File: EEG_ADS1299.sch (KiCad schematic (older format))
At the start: 76 parts, among them IC1 ADS1299, P1 CONN_2, P2 CONN_2, P3 CONN_01X08, U1 TPS2294x, U2 TPS61222, U3 NRF528XX-QFAA, U4 MPU-9250, U5 INA828, U6 INA828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

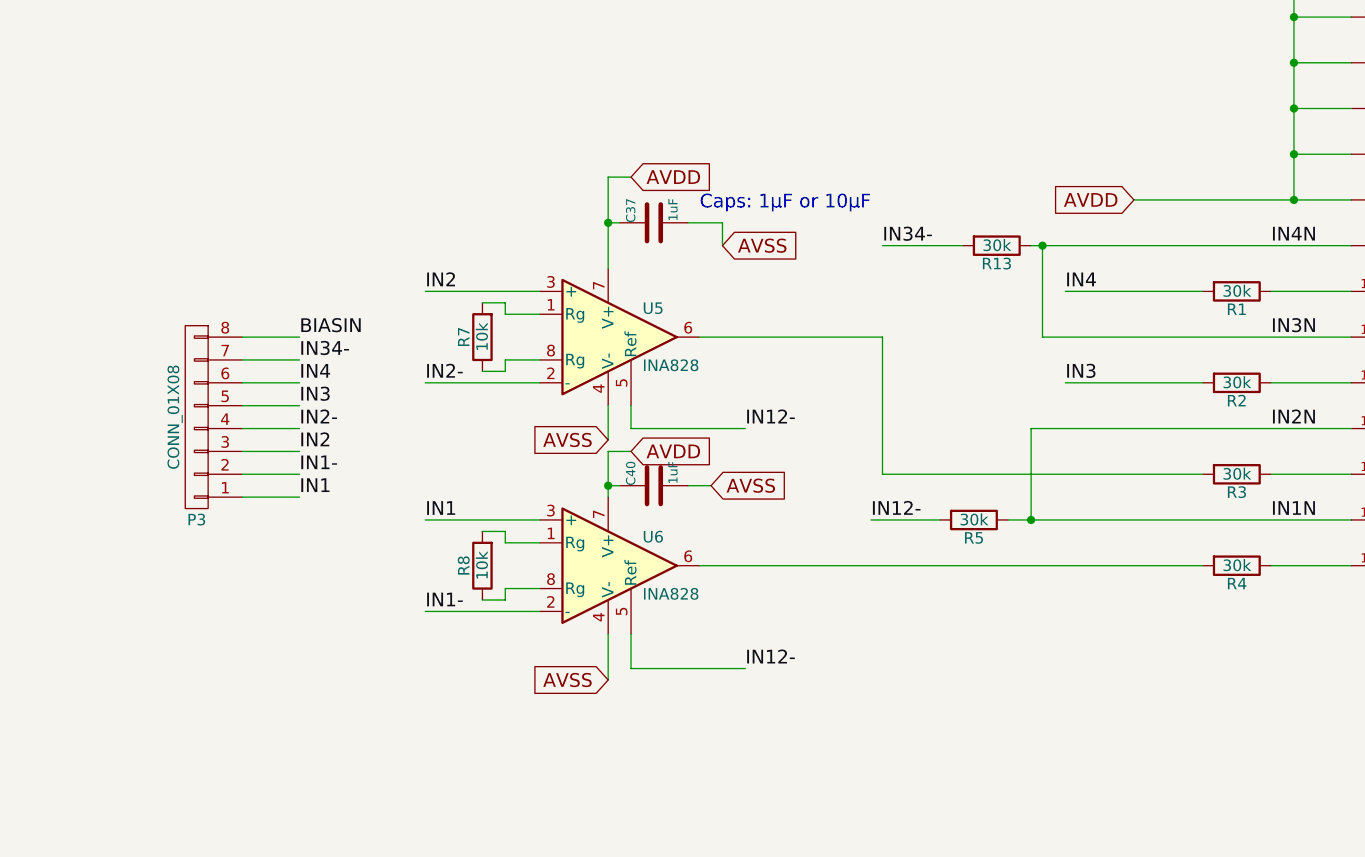
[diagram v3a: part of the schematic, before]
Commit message: Update Schematic for ADS1299/INA828 Removing INA828 from circuit. Shorting negative inputs in pairs.
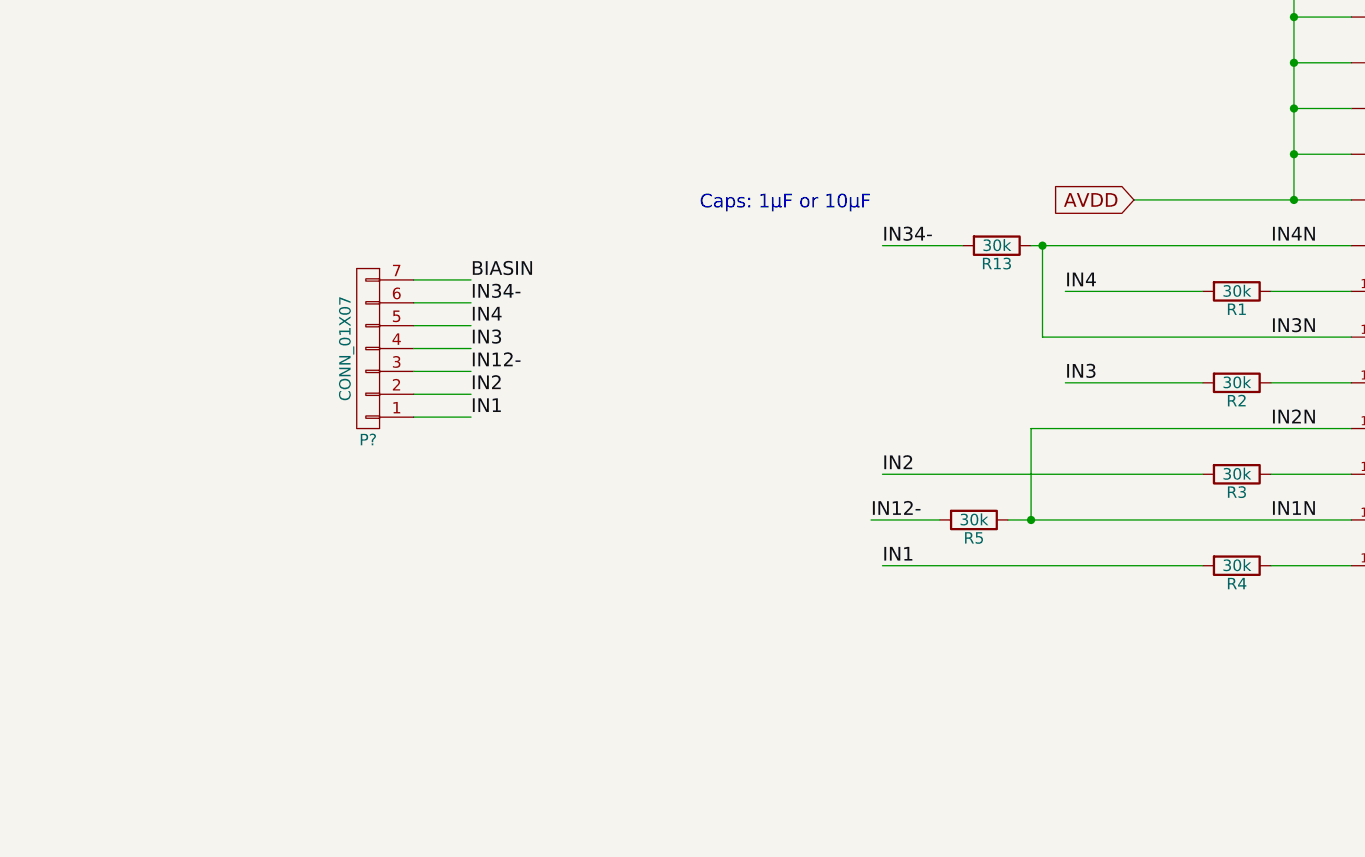
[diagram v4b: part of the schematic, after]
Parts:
- removed C37, C40: 1uF, Capacitors_SMD:C_0402, symbol C
- removed P3: CONN_01X08, symbol CONN_01X08
- removed R7, R8: 10k, Resistors_SMD:R_0402, symbol R
- removed U5, U6: INA828, INA828:SOIC_8_4.9mm_x_3.91, symbol INA128
- added P?: CONN_01X07, symbol CONN_01X07
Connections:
- net BIASIN: now also P?.7 (P7)
- net IN1: now also R4.2, P?.1 (P1)
- net IN12-: now also P?.3 (P3)
- net IN2: now also R3.2, P?.2 (P2)
- net IN3: now also P?.4 (P4)
- net IN34-: now also P?.6 (P6)
- net IN4: now also P?.5 (P5)
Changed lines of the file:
@@
 Text Label 13500 10050 0    60   ~ 0
 IN4N
-Text Label 9250 10850 0    60   ~ 0
-IN2-
-Text Label 9250 11050 0    60   ~ 0
-IN1-
 $Comp
 L NRF528XX-QFAA-RESCUE-EEG_ADS1299_2 U3
@@
 Text Label 11750 11250 0    60   ~ 0
 IN12-
-$Comp
-L INA128 U5
-U 1 1 5A26481D
-P 10600 10450
-F 0 "U5" H 10750 10575 50  0000 L CNN
-F 1 "INA828" H 10750 10325 50  0000 L CNN
-F 2 "INA828:SOIC_8_4.9mm_x_3.91" H 10700 10450 50  0001 C CNN
-F 3 "" H 10700 10450 50  0001 C CNN
-	1    10600 10450
-	1    0    0    -1
-$EndComp
-$Comp
-L INA128 U6
-U 1 1 5A265779
-P 10600 11450
-F 0 "U6" H 10750 11575 50  0000 L CNN
-F 1 "INA828" H 10750 11325 50  0000 L CNN
-F 2 "INA828:SOIC_8_4.9mm_x_3.91" H 10700 11450 50  0001 C CNN
-F 3 "" H 10700 11450 50  0001 C CNN
-	1    10600 11450
-	1    0    0    -1
-$EndComp
-Text GLabel 10600 10900 0    60   Input ~ 0
-AVSS
-Text GLabel 10600 11950 0    60   Input ~ 0
-AVSS
-Text GLabel 10700 10950 2    60   Input ~ 0
-AVDD
-Text GLabel 10700 9750 2    60   Input ~ 0
-AVDD
-$Comp
-L R R7
-U 1 1 5A26B635
-P 10050 10450
-F 0 "R7" V 10130 10450 50  0000 C CNN
-F 1 "10k" V 10050 10450 50  0000 C CNN
-F 2 "Resistors_SMD:R_0402" V 9980 10450 50  0001 C CNN
-F 3 "" H 10050 10450 50  0000 C CNN
-	1    10050 10450
-	-1   0    0    1
-$EndComp
-$Comp
-L R R8
-U 1 1 5A26CFB1
-P 10050 11450
-F 0 "R8" V 10130 11450 50  0000 C CNN
-F 1 "10k" V 10050 11450 50  0000 C CNN
-F 2 "Resistors_SMD:R_0402" V 9980 11450 50  0001 C CNN
-F 3 "" H 10050 11450 50  0000 C CNN
-	1    10050 11450
-	-1   0    0    1
-$EndComp
-Text Label 9800 11250 0    60   ~ 0
+Text Label 10000 10500 0    60   ~ 0
+IN3
+Text Label 10000 10700 0    60   ~ 0
+IN2
+Text Label 10000 10800 0    60   ~ 0
 IN1
-Text Label 9800 10250 0    60   ~ 0
-IN2
-Text Label 9250 10650 0    60   ~ 0
-IN4
-Text Label 9250 10750 0    60   ~ 0
-IN3
-Text Label 9250 10950 0    60   ~ 0
-IN2
-Text Label 9250 11150 0    60   ~ 0
-IN1
-Text Label 9250 10450 0    60   ~ 0
+Text Label 10000 10200 0    60   ~ 0
 BIASIN
 Text Label 13500 10450 0    60   ~ 0
 IN3N
-$Comp
-L C C37
-U 1 1 5A28A53A
-P 10800 9950
-F 0 "C37" H 10800 10050 40  0000 L CNN
-F 1 "1uF" H 10806 9865 40  0000 L CNN
-F 2 "Capacitors_SMD:C_0402" H 10838 9800 30  0001 C CNN
-F 3 "~" H 10800 9950 60  0000 C CNN
-	1    10800 9950
-	0    -1   -1   0
-$EndComp
-Text GLabel 11100 10050 2    60   Input ~ 0
-AVSS
 Text Notes 11000 9900 0    60   ~ 0
 Caps: 1µF or 10µF
@@
 	1    0    0    -1
 $EndComp
-Wire Wire Line
-	11800 10450 11800 11050
-Wire Wire Line
-	11000 10450 11800 10450
-Wire Wire Line
-	10300 11250 9800 11250
-Wire Wire Line
-	10150 11600 10150 11550
-Wire Wire Line
-	10050 11600 10150 11600
-Wire Wire Line
-	10150 11550 10300 11550
-Wire Wire Line
-	10150 11300 10050 11300
-Wire Wire Line
-	10150 11350 10150 11300
-Wire Wire Line
-	10300 11350 10150 11350
-Wire Wire Line
-	10300 10250 9800 10250
-Wire Wire Line
-	10150 10300 10050 10300
-Wire Wire Line
-	10150 10350 10150 10300
-Wire Wire Line
-	10300 10350 10150 10350
-Wire Wire Line
-	10150 10550 10300 10550
-Wire Wire Line
-	10150 10600 10150 10550
-Wire Wire Line
-	10050 10600 10150 10600
-Wire Wire Line
-	10600 9750 10600 10150
-Wire Wire Line
-	10600 10950 10600 11150
-Wire Wire Line
-	10700 11900 11200 11900
-Wire Wire Line
-	10700 11750 10700 11900
-Wire Wire Line
-	10700 10850 11200 10850
-Wire Wire Line
-	10700 10750 10700 10850
-Wire Wire Line
-	10600 11750 10600 11950
-Wire Wire Line
-	10600 10750 10600 10900
-Wire Wire Line
-	11000 11450 13200 11450
 Connection ~ 2450 6800
 Wire Wire Line
@@
 	23800 5700 23800 6850
 Wire Wire Line
-	9800 10650 10300 10650
-Wire Wire Line
-	9000 10550 9250 10550
-Wire Wire Line
-	9000 10650 9250 10650
-Wire Wire Line
-	9000 10750 9250 10750
-Wire Wire Line
-	9000 10850 9250 10850
-Wire Wire Line
-	9000 11050 9250 11050
-Wire Wire Line
-	9000 11150 9250 11150
-Wire Wire Line
-	10600 9750 10700 9750
-Wire Wire Line
-	10600 9950 10650 9950
-Connection ~ 10600 9950
-Wire Wire Line
-	10950 9950 11100 9950
-Wire Wire Line
-	11100 9950 11100 10050
-Wire Wire Line
-	10600 10950 10700 10950
+	9750 10200 10000 10200
+Wire Wire Line
+	9750 10300 10000 10300
+Wire Wire Line
+	9750 10400 10000 10400
+Wire Wire Line
+	9750 10500 10000 10500
+Wire Wire Line
+	9750 10700 10000 10700
+Wire Wire Line
+	9750 10800 10000 10800
 Wire Wire Line
 	7800 3550 8800 3550
@@
 Text Label 3300 3300 0    60   ~ 0
 Vout
-$Comp
-L C C40
-U 1 1 5A305D06
-P 10800 11100
-F 0 "C40" H 10800 11200 40  0000 L CNN
-F 1 "1uF" H 10806 11015 40  0000 L CNN
-F 2 "Capacitors_SMD:C_0402" H 10838 10950 30  0001 C CNN
-F 3 "~" H 10800 11100 60  0000 C CNN
-	1    10800 11100
-	0    -1   -1   0
-$EndComp
-Text GLabel 11050 11100 2    60   Input ~ 0
-AVSS
-Wire Wire Line
-	11050 11100 10950 11100
-Wire Wire Line
-	10650 11100 10600 11100
-Connection ~ 10600 11100
 Text Label 13500 11250 0    60   ~ 0
 IN1N
@@
 IN2N
 Wire Wire Line
-	9000 10950 9250 10950
-Wire Wire Line
-	10300 11650 9800 11650
-Text Label 9800 11650 0    60   ~ 0
-IN1-
-Text Label 9800 10650 0    60   ~ 0
-IN2-
+	9750 10600 10000 10600
 Wire Wire Line
 	12450 11250 12450 10850
@@
 Text Label 11800 10050 0    60   ~ 0
 IN34-
-Text Label 11200 10850 0    60   ~ 0
-IN12-
-Text Label 11200 11900 0    60   ~ 0
-IN12-
 Wire Wire Line
 	12500 10450 13850 10450
@@
 	12500 10050 12500 10450
 Connection ~ 12500 10050
-Wire Wire Line
-	9250 10450 9000 10450
-Text Label 9250 10550 0    60   ~ 0
+Text Label 10000 10300 0    60   ~ 0
 IN34-
-$Comp
-L CONN_01X08 P3
-U 1 1 5A321A4A
-P 8800 10800
-F 0 "P3" H 8800 11250 50  0000 C CNN
-F 1 "CONN_01X08" V 8900 10800 50  0000 C CNN
-F 2 "" H 8800 10800 50  0000 C CNN
-F 3 "" H 8800 10800 50  0000 C CNN
-	1    8800 10800
+Wire Wire Line
+	13200 11450 11800 11450
+Text Label 10000 10600 0    60   ~ 0
+IN12-
+$Comp
+L CONN_01X07 P?
+U 1 1 5A54961F
+P 9550 10500
+F 0 "P?" H 9550 10900 50  0000 C CNN
+F 1 "CONN_01X07" V 9650 10500 50  0000 C CNN
+F 2 "" H 9550 10500 50  0000 C CNN
+F 3 "" H 9550 10500 50  0000 C CNN
+	1    9550 10500
 	-1   0    0    1
 $EndComp
+Text Label 11800 11450 0    60   ~ 0
+IN1
+Text Label 11800 11050 0    60   ~ 0
+IN2
+Text Label 10000 10400 0    60   ~ 0
+IN4
 $EndSCHEMATC

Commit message: Revert to old design.
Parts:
- removed P?: CONN_01X07, symbol CONN_01X07
- added P?: CONN_01X02, symbol CONN_01X02
- added P?: CONN_01X08, symbol CONN_01X08
- renumbered R13 to R7
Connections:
- net AVDD: now also P?.2 (P2)
- net BIASIN: now also P?.8 (P8)
- net GND: now also P?.1 (P1)
- net IN1: now also P?.2 (P2)
- net IN12-: now also P?.4 (P4)
- net IN2: now also P?.3 (P3)
- net IN3: now also P?.5 (P5)
- net IN34-: now also P?.7 (P7)
- net IN4: now also P?.6 (P6)
- net SRB1: now reaches IC1.17 (SRB1)
- net SRB1: now also P?.1 (P1)
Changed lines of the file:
@@
 This network will need to be tuned
 $Comp
-L GND-RESCUE-emg_circuit_2_ext_amp #PWR2
+L GND-RESCUE-emg_circuit_2_ext_amp #PWR01
 U 1 1 588ADF4E
 P 2450 7150
-F 0 "#PWR2" H 2450 7150 30  0001 C CNN
+F 0 "#PWR01" H 2450 7150 30  0001 C CNN
 F 1 "GND" H 2450 7080 30  0001 C CNN
 F 2 "" H 2450 7150 60  0000 C CNN
@@
 $EndComp
 $Comp
-L VCC #PWR1
+L VCC #PWR02
 U 1 1 588ADF4F
 P 2450 6700
-F 0 "#PWR1" H 2450 6800 30  0001 C CNN
+F 0 "#PWR02" H 2450 6800 30  0001 C CNN
 F 1 "VCC" H 2450 6800 30  0000 C CNN
 F 2 "" H 2450 6700 60  0000 C CNN
@@
 $EndComp
 $Comp
-L GND-RESCUE-emg_circuit_2_ext_amp #PWR5
+L GND-RESCUE-emg_circuit_2_ext_amp #PWR03
 U 1 1 589975BD
 P 13400 3250
-F 0 "#PWR5" H 13400 3250 30  0001 C CNN
+F 0 "#PWR03" H 13400 3250 30  0001 C CNN
 F 1 "GND" H 13400 3180 30  0001 C CNN
 F 2 "" H 13400 3250 60  0000 C CNN
@@
 $EndComp
 $Comp
-L VCC #PWR3
+L VCC #PWR04
 U 1 1 58A71443
 P 10000 1350
-F 0 "#PWR3" H 10000 1450 30  0001 C CNN
+F 0 "#PWR04" H 10000 1450 30  0001 C CNN
 F 1 "VCC" H 10000 1450 30  0000 C CNN
 F 2 "" H 10000 1350 60  0000 C CNN
@@
 DGND
 $Comp
-L GND-RESCUE-emg_circuit_2_ext_amp #PWR6
+L GND-RESCUE-emg_circuit_2_ext_amp #PWR05
 U 1 1 58B4A72D
 P 13900 4050
-F 0 "#PWR6" H 13900 4050 30  0001 C CNN
+F 0 "#PWR05" H 13900 4050 30  0001 C CNN
 F 1 "GND" H 13900 3980 30  0001 C CNN
 F 2 "" H 13900 4050 60  0000 C CNN
@@
 	0    1    1    0
 $EndComp
-Text Label 11750 11250 0    60   ~ 0
+Text Label 11800 11250 0    60   ~ 0
 IN12-
 Text Label 10000 10500 0    60   ~ 0
@@
 DGND
 $Comp
-L GND-RESCUE-emg_circuit_2_ext_amp #PWR4
+L GND-RESCUE-emg_circuit_2_ext_amp #PWR06
 U 1 1 5A313557
 P 11650 3950
-F 0 "#PWR4" H 11650 3950 30  0001 C CNN
+F 0 "#PWR06" H 11650 3950 30  0001 C CNN
 F 1 "GND" H 11650 3880 30  0001 C CNN
 F 2 "" H 11650 3950 60  0000 C CNN
@@
 	12450 11250 12450 10850
 Connection ~ 12450 11250
-Wire Wire Line
-	12050 11250 11750 11250
 Text Label 11800 10050 0    60   ~ 0
 IN34-
@@
 	12500 10450 13850 10450
 $Comp
-L R R13
+L R R7
 U 1 1 5A31B95B
 P 12300 10050
-F 0 "R13" V 12380 10050 50  0000 C CNN
+F 0 "R7" V 12380 10050 50  0000 C CNN
 F 1 "30k" V 12300 10050 50  0000 C CNN
 F 2 "Resistors_SMD:R_0402" V 12230 10050 50  0001 C CNN
@@
 Text Label 10000 10600 0    60   ~ 0
 IN12-
-$Comp
-L CONN_01X07 P?
-U 1 1 5A54961F
-P 9550 10500
-F 0 "P?" H 9550 10900 50  0000 C CNN
-F 1 "CONN_01X07" V 9650 10500 50  0000 C CNN
-F 2 "" H 9550 10500 50  0000 C CNN
-F 3 "" H 9550 10500 50  0000 C CNN
-	1    9550 10500
-	-1   0    0    1
-$EndComp
 Text Label 11800 11450 0    60   ~ 0
 IN1
@@
 Text Label 10000 10400 0    60   ~ 0
 IN4
+Wire Wire Line
+	12050 11250 11800 11250
+$Comp
+L CONN_01X02 P?
+U 1 1 5A54E74E
+P 9550 11250
+F 0 "P?" H 9550 11400 50  0000 C CNN
+F 1 "CONN_01X02" V 9650 11250 50  0000 C CNN
+F 2 "" H 9550 11250 50  0000 C CNN
+F 3 "" H 9550 11250 50  0000 C CNN
+	1    9550 11250
+	-1   0    0    1
+$EndComp
+Wire Wire Line
+	9750 11200 10200 11200
+$Comp
+L CONN_01X08 P?
+U 1 1 5A54F52F
+P 9550 10550
+F 0 "P?" H 9550 11000 50  0000 C CNN
+F 1 "CONN_01X08" V 9650 10550 50  0000 C CNN
+F 2 "" H 9550 10550 50  0000 C CNN
+F 3 "" H 9550 10550 50  0000 C CNN
+	1    9550 10550
+	-1   0    0    1
+$EndComp
+Wire Wire Line
+	9750 10900 10000 10900
+Wire Wire Line
+	14350 12000 14350 12150
+Wire Wire Line
+	14350 12150 11850 12150
+Text Label 11850 12150 0    60   ~ 0
+SRB1
+Text Label 10000 10900 0    60   ~ 0
+SRB1
+Wire Wire Line
+	9750 11300 10200 11300
+Text GLabel 10200 11300 2    60   Input ~ 0
+AVSS
+Text GLabel 10200 11200 2    60   Input ~ 0
+AVDD
 $EndSCHEMATC
